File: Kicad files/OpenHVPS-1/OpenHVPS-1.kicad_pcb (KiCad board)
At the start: 2 copper layers, 77.5 x 20.5 mm, 67 parts, among them J1 Conn_01x03_Male, J2 Conn_01x03_Male, Q1 FQT7N10, Q2 BC846, Q3 MMDT3906, U1 74HC14, U2 MAX4162, U3 CD14538BM, U4 MAX6008AEUR+T

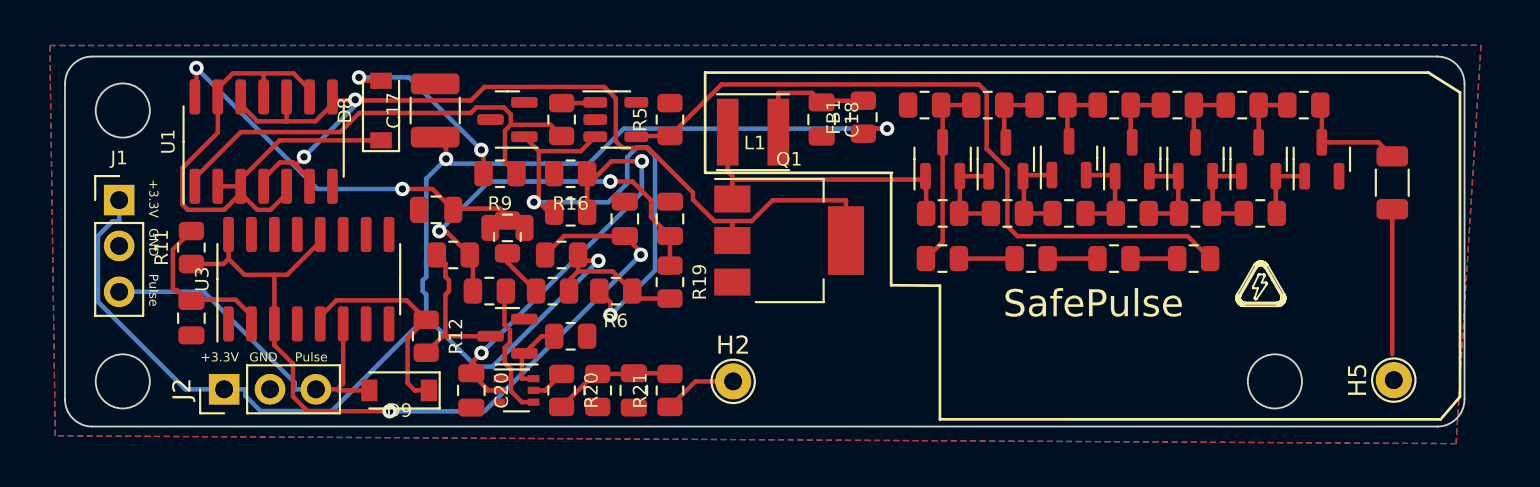
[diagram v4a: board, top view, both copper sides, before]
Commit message: Replaced foot prints of anaode/cathode and text
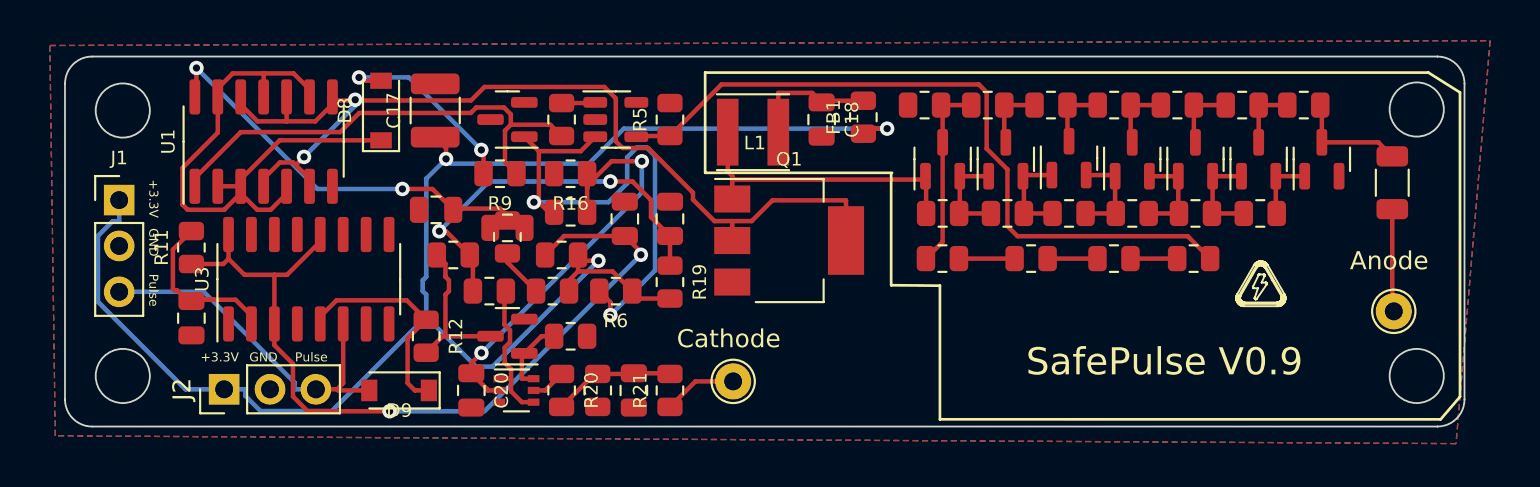
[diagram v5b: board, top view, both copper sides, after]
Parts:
- moved H5 3.81 mm to (164.1, 71.1)
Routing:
- net Net-(H5-Pad1): track 8.04 -> 5.69 mm
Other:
- outline, holes or cut-outs redrawn
- board text added: "SafePulse V0.9"
- board text removed: "SafePulse"
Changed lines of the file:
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@@
     (pad "3" thru_hole oval (at 0 5.08 90) (locked) (size 1.7 1.7) (drill 1) (layers *.Cu *.Mask)
       (net 24 "Net-(D9-Pad2)") (pinfunction "Pin_3"))
-    (model "${KICAD6_3DMODEL_DIR}/Connector_PinHeader_2.54mm.3dshapes/PinHeader_1x03_P2.54mm_Vertical.wrl"
+    (model "${KICAD6_3DMODEL_DIR}/Connector_PinHeader_2.54mm.3dshapes/PinHeader_1x03_P2.54mm_Vertical.wrl" hide
       (offset (xyz 0 0 -2))
       (scale (xyz 1 1 1))
       (rotate (xyz 0 -180 0))
     )
+    (model "${KICAD6_3DMODEL_DIR}/Connector_PinHeader_2.54mm.3dshapes/PinHeader_1x03_P2.54mm_Horizontal.wrl" hide
+      (offset (xyz 0 -5 0))
+      (scale (xyz 1 1 1))
+      (rotate (xyz 0 0 -180))
+    )
   )
   (footprint "TestPoint:TestPoint_THTPad_D2.0mm_Drill1.0mm" (layer "F.Cu")
-    (at 164.084 74.93 90)
+    (at 164.084 71.12 90)
     (descr "THT pad as test Point, diameter 2.0mm, hole diameter 1.0mm")
     (tags "test point THT pad")
@@
     (property "Sheet name" "")
     (attr exclude_from_pos_files exclude_from_bom)
-    (fp_text reference "H5" (at 0 -1.998 90) (layer "F.SilkS")
+    (fp_text reference "H5" (at 0 -1.998 90) (layer "F.SilkS") hide
       (effects (font (size 1 1) (thickness 0.15)))
     )
-    (fp_text value "Anode" (at 0 2.05 90) (layer "F.Fab")
+    (fp_text value "Anode" (at 2.794 -0.254 180) (layer "F.SilkS")
       (effects (font (size 1 1) (thickness 0.15)))
     )
-    (fp_text user "${REFERENCE}" (at 0 -2 90) (layer "F.Fab")
+    (fp_text user "${VALUE}" (at 2.54 -0.254) (layer "B.SilkS")
+      (effects (font (size 1 1) (thickness 0.15)) (justify mirror))
+    )
+    (fp_text user "${REFERENCE}" (at 0 -2 90) (layer "F.Fab") hide
       (effects (font (size 1 1) (thickness 0.15)))
     )
@@
     (property "Sheet name" "")
     (attr exclude_from_pos_files exclude_from_bom)
-    (fp_text reference "H2" (at 0 -1.998) (layer "F.SilkS")
+    (fp_text reference "H2" (at 0 -1.998) (layer "F.SilkS") hide
       (effects (font (size 1 1) (thickness 0.15)))
     )
-    (fp_text value "Cathode" (at 0 2.05) (layer "F.Fab")
+    (fp_text value "Cathode" (at -0.246 -2.356) (layer "F.SilkS")
       (effects (font (size 1 1) (thickness 0.15)))
     )
-    (fp_text user "${REFERENCE}" (at 0 -2) (layer "F.Fab")
+    (fp_text user "${VALUE}" (at 0.516 -2.356) (layer "B.SilkS")
+      (effects (font (size 1 1) (thickness 0.15)) (justify mirror))
+    )
+    (fp_text user "${REFERENCE}" (at 0 -2) (layer "F.Fab") hide
       (effects (font (size 1 1) (thickness 0.15)))
     )
@@
     (pad "3" thru_hole oval (at 0 5.08) (locked) (size 1.7 1.7) (drill 1) (layers *.Cu *.Mask)
       (net 24 "Net-(D9-Pad2)") (pinfunction "Pin_3"))
-    (model "${KICAD6_3DMODEL_DIR}/Connector_PinHeader_2.54mm.3dshapes/PinHeader_1x03_P2.54mm_Vertical.wrl"
+    (model "${KICAD6_3DMODEL_DIR}/Connector_PinHeader_2.54mm.3dshapes/PinHeader_1x03_P2.54mm_Vertical.wrl" hide
       (offset (xyz 0 0 -2))
       (scale (xyz 1 1 1))
@@
   (gr_line (start 157.64519 70.708462) (end 157.666527 70.707773) (layer "F.SilkS") (width 0.104))
   (gr_line (start 157.675118 70.835318) (end 157.660201 70.836043) (layer "F.SilkS") (width 0.104))
-  (gr_circle (center 93.7 75) (end 95.2 75) (layer "Edge.Cuts") (width 0.1) (fill none))
+  (gr_circle (center 93.7 74.7) (end 95.2 74.7) (layer "Edge.Cuts") (width 0.1) (fill none))
   (gr_arc (start 166.5 76) (end 168 76) (angle 90) (layer "Edge.Cuts") (width 0.1))
   (gr_line (start 166.5 77.5) (end 92 77.5) (layer "Edge.Cuts") (width 0.1))
   (gr_line (start 168 58.51066) (end 168 76) (layer "Edge.Cuts") (width 0.1))
+  (gr_circle (center 165.354 74.7) (end 166.854 74.7) (layer "Edge.Cuts") (width 0.1) (fill none))
   (gr_arc (start 166.5 58.51066) (end 166.5 57.01066) (angle 90) (layer "Edge.Cuts") (width 0.1))
   (gr_arc (start 92 76) (end 92 77.5) (angle 90) (layer "Edge.Cuts") (width 0.1))
   (gr_line (start 92 57.01066) (end 166.5 57.01066) (layer "Edge.Cuts") (width 0.1))
-  (gr_circle (center 157.5 75) (end 159 75) (layer "Edge.Cuts") (width 0.1) (fill none))
+  (gr_circle (center 165.354 59.944) (end 166.854 59.944) (layer "Edge.Cuts") (width 0.1) (fill none))
   (gr_line (start 90.5 76) (end 90.5 58.51066) (layer "Edge.Cuts") (width 0.1))
   (gr_circle (center 93.7 60) (end 95.2 60) (layer "Edge.Cuts") (width 0.1) (fill none))
   (gr_arc (start 92 58.51066) (end 90.5 58.51066) (angle 90) (layer "Edge.Cuts") (width 0.1))
-  (gr_text "SafePulse " (at 146.25 70.45) (layer "B.SilkS")
-    (effects (font (size 1.5 1.5) (thickness 0.15)) (justify mirror))
+  (gr_text "GND\n" (at 95.3825 67.434762 270) (layer "B.SilkS")
+    (effects (font (size 0.5 0.5) (thickness 0.1)) (justify mirror))
+  )
+  (gr_text "+3.3V" (at 95.3825 69.854761 270) (layer "B.SilkS")
+    (effects (font (size 0.5 0.5) (thickness 0.1)) (justify mirror))
+  )
+  (gr_text "+3.3V" (at 99.07 73.6775) (layer "B.SilkS")
+    (effects (font (size 0.5 0.5) (thickness 0.1)) (justify mirror))
+  )
+  (gr_text "Pulse" (at 104.14 73.6775) (layer "B.SilkS")
+    (effects (font (size 0.5 0.5) (thickness 0.1)) (justify mirror))
+  )
+  (gr_text "GND\n" (at 101.49 73.6775) (layer "B.SilkS")
+    (effects (font (size 0.5 0.5) (thickness 0.1)) (justify mirror))
+  )
+  (gr_text "Pulse" (at 95.3825 64.784761 270) (layer "B.SilkS")
+    (effects (font (size 0.5 0.5) (thickness 0.1)) (justify mirror))
   )
-  (gr_text "SafePulse " (at 147.45 70.7) (layer "F.SilkS")
+  (gr_text "SafePulse V0.9" (at 151.384 73.914) (layer "F.SilkS")
     (effects (font (size 1.5 1.5) (thickness 0.15)))
   )
@@
   (segment (start 127.5 75) (end 125.4125 75) (width 0.25) (layer "F.Cu") (net 48))
   (segment (start 125.4125 75) (end 124 76.4125) (width 0.25) (layer "F.Cu") (net 48))
-  (segment (start 164 65.4625) (end 164 73.5) (width 0.25) (layer "F.Cu") (net 49))
+  (segment (start 164 71.036) (end 164.084 71.12) (width 0.25) (layer "F.Cu") (net 49))
+  (segment (start 164 65.4625) (end 164 71.036) (width 0.25) (layer "F.Cu") (net 49))
   (zone (net 3) (net_name "GND") (layers F&B.Cu) (hatch edge 0.508)
     (connect_pads (clearance 0.508))
@@
         (xy 89.959933 78.015183)
         (xy 89.662 56.4)
-        (xy 168.91 56.388)
+        (xy 169.418 56.134)
       )
     )

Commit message: moved components around to shorten tracks, trying to keep layout   critical stuff together
  Please enter the commit message for your changes. Lines starting
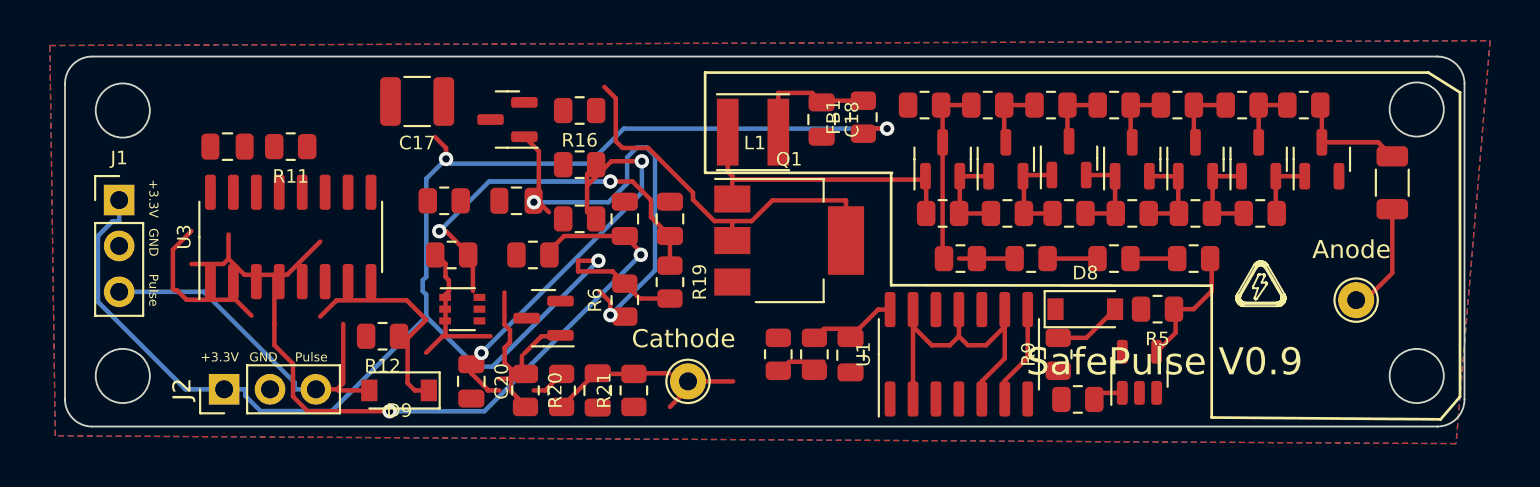
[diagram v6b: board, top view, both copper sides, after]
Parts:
- moved D8 40.5 mm to (147.0, 71.0), turned to 0 degrees
- moved U1 40.3 mm to (140.0, 73.5)
- moved R8 32.5 mm to (146.6, 76.0), turned to 0 degrees
- moved R9 32.5 mm to (145.5, 73.5), turned to 90 degrees
- moved U2 32.2 mm to (150.0, 74.5), turned to 90 degrees
- moved R5 29.0 mm to (151.0, 71.0), turned to 180 degrees
- moved C15 24.3 mm to (134.0, 73.5), turned to -90 degrees
- moved R10 18.2 mm to (132.0, 73.5)
- moved FB2 13.0 mm to (130.0, 73.5), turned to -90 degrees
- moved C16 9.71 mm to (99.5, 62.0), turned to 180 degrees
- moved R11 7.84 mm to (103.0, 62.0), turned to 180 degrees
- moved Q3 5.41 mm to (112.5, 71.0)
- moved R17 4.96 mm to (116.4, 68.0)
- moved R16 3.54 mm to (119.0, 60.0)
- moved R14 3.04 mm to (111.5, 65.0)
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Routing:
- net Net-(R4-Pad1): track 40.6 -> 7.17 mm
- net Net-(Q1-Pad2): track 54.4 -> 27.3 mm, vias 2 -> 0
- net Net-(C14-Pad1): track 26.5 -> 0.00 mm
- net Net-(C15-Pad1): track 22.6 -> 4.13 mm, vias 2 -> 0
- net Net-(D8-Pad1): track 32.9 -> 19.2 mm
- net Net-(C16-Pad1): track 10.3 -> 0.00 mm
- net GND: track 0.00 -> 8.59 mm
- net Net-(D8-Pad2): track 11.1 -> 3.81 mm, vias 2 -> 0
- net +2V5: track 29.2 -> 25.5 mm
- net +3V3: track 89.1 -> 87.1 mm
- net Net-(Q3-Pad5): track 1.94 -> 0.00 mm
- net Net-(C22-Pad1): track 6.79 -> 8.44 mm
- net Net-(FB2-Pad2): track 2.75 -> 1.91 mm

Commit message: Routed board.
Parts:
- turned C22 to 90 degrees
- turned R21 to -90 degrees
- turned R22 to 90 degrees
- turned R5 to 0 degrees
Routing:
- net GND: track 8.59 -> 89.3 mm, vias 0 -> 7
- net Net-(C14-Pad1): track 0.00 -> 45.4 mm, vias 0 -> 3
- net +2V5: track 25.5 -> 47.1 mm
- net Net-(Q2-Pad3): track 8.80 -> 25.6 mm, vias 0 -> 2
- net Net-(Q1-Pad2): track 27.3 -> 41.7 mm
- net Net-(C19-Pad1): track 46.3 -> 33.0 mm, vias 2 -> 0
- net Net-(D9-Pad2): track 20.1 -> 32.1 mm
- net Net-(C16-Pad1): track 0.00 -> 11.6 mm
- net +3V3: track 87.1 -> 96.5 mm, vias 3 -> 0
- net Net-(D8-Pad1): track 19.2 -> 25.2 mm, vias 0 -> 3
- net Net-(Q3-Pad5): track 0.00 -> 5.02 mm
- net Net-(Q2-Pad1): track 3.96 -> 7.85 mm
- net Net-(Q3-Pad1): track 8.02 -> 5.46 mm
- net Net-(C22-Pad1): track 8.44 -> 6.03 mm
- net Net-(C20-Pad1): track 23.3 -> 21.1 mm
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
